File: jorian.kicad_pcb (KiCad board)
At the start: 2 copper layers, 99.1 x 99.7 mm, 107 parts, among them J1 MicroUSB, J2 USB-C, J3 MicroUSB, J4 USB-C, J5 MJ-4PP-9, SW1 SW_SPDT, U3 AMS1117, U4 TP4056, U5 DW01A, U6 FS8205A

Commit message: updated placement
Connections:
- J4 pad A6: D+ -> Net-(J4-PadA6)
- J4 pad A7: D- -> Net-(J4-PadA7)
- J4 pad B6: D+ -> Net-(J4-PadA6)
- J4 pad B7: D- -> Net-(J4-PadA7)
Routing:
- net VCC: track 608.3 -> 683.9 mm, vias 28 -> 23
- net Net-(JP4-Pad2): track 84.2 -> 149.1 mm, vias 2 -> 3
- net SCL: track 139.5 -> 94.7 mm, vias 11 -> 3
- net LIPO+: track 76.6 -> 113.3 mm, vias 3 -> 7
- net /S2: track 110.6 -> 77.9 mm, vias 7 -> 5
- net /S5: track 111.5 -> 79.8 mm, vias 6 -> 4
- net /S21: track 91.5 -> 109.7 mm
- net Net-(JP3-Pad2): track 131.8 -> 145.8 mm
- net /S12: track 47.7 -> 35.2 mm, vias 3 -> 2
- net /S18: track 63.5 -> 51.3 mm, vias 3 -> 2
- net Net-(L7-Pad1): track 36.0 -> 48.0 mm, vias 3 -> 2
- net SWO: track 56.6 -> 45.6 mm
- net /S19: track 126.2 -> 116.5 mm, vias 4 -> 3
- net /DIN18: track 13.6 -> 21.8 mm, vias 1 -> 0
- net Net-(U5-Pad1): track 32.2 -> 40.3 mm
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
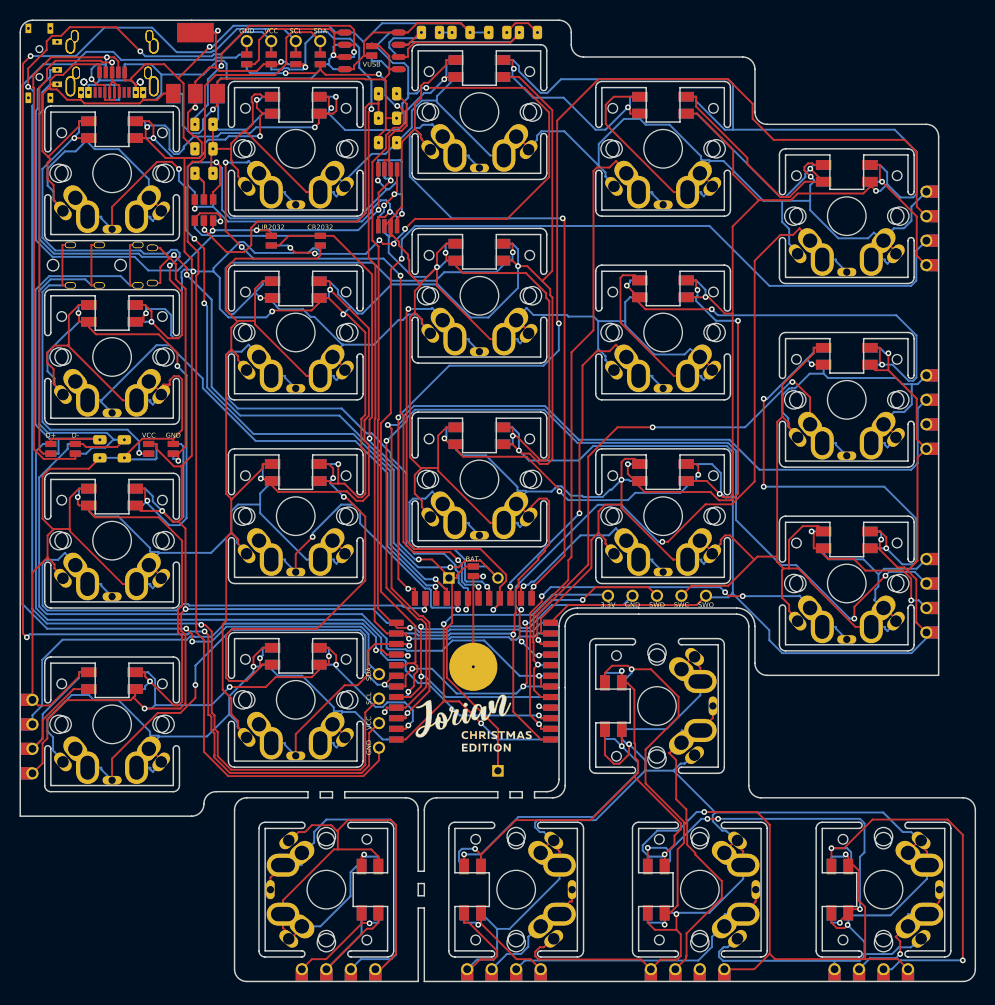
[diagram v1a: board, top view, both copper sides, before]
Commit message: separate charger
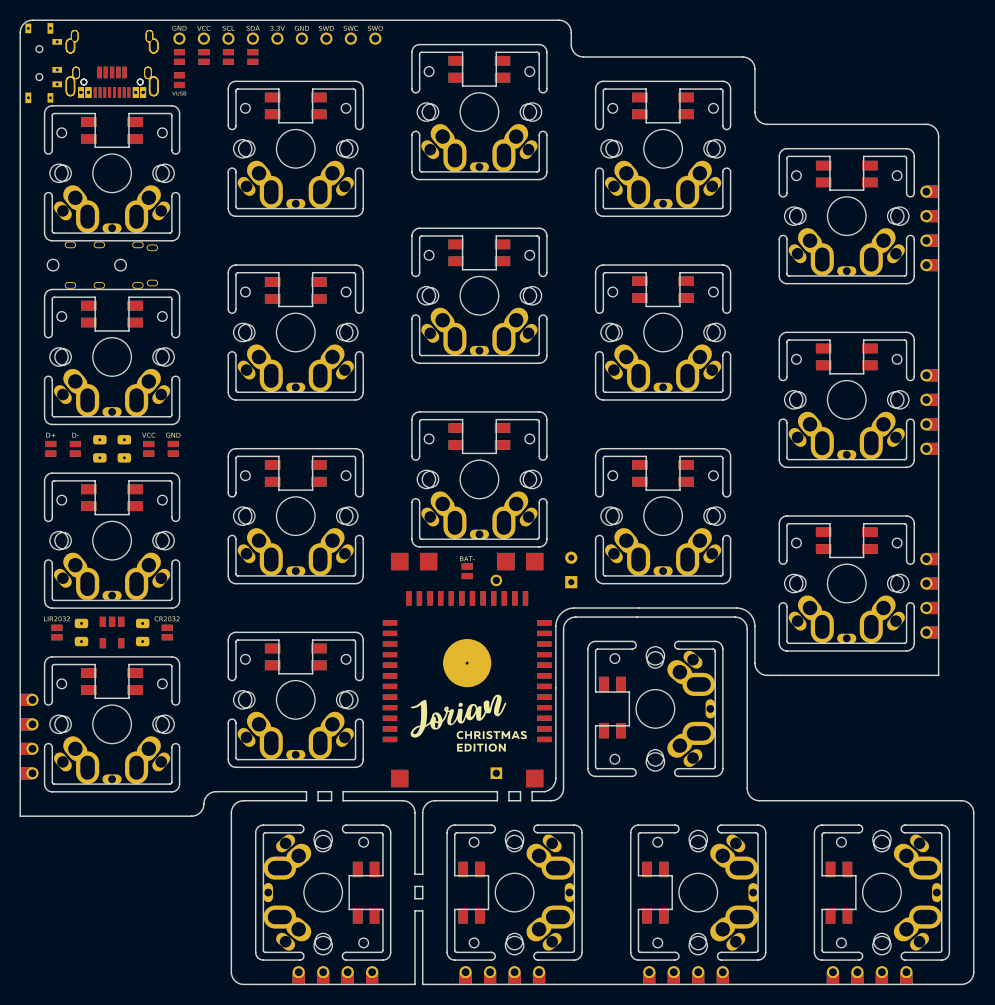
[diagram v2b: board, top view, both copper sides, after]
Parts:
- removed C3, C4: 0.1uF, kbd:C_0805
- removed C5: 10uF, kbd:C_0805
- removed D1, D2: LED, kbd:R_0805
- removed OLED2: I2C_conn, kbd:connector_i2c
- removed R1: 1.2K, kbd:R_0805
- removed R2, R6, R7: 1K, kbd:R_0805
- removed R3: 100, kbd:R_0805
- removed U4: TP4056, kbd:SOP-8
- removed U5: DW01A, kbd:SOT-23-6
- removed U6: FS8205A, kbd:TSSOP-8
- added C1: 1nF, kbd:C_0805, F.Cu at (47.6, 102.2)
- added C2: 1nF, kbd:C_0805, F.Cu at (54.0, 102.2)
- added J6: lipo_charger, kbd:lipo_charger_03962A, F.Cu at (87.6, 119.4)
- added J7: lipo_header, kbd:lipo_header, F.Cu at (98.4, 95.8)
- U3: value AMS1117 -> LP3990-3.3v; footprint kbd:SOT-223-3 -> kbd:SOT-23-5
- moved JP16 67.2 mm to (71.8, 40.6)
- moved U3 59.7 mm to (50.8, 102.2), turned to 270 degrees
- moved JP18 46.3 mm to (45.1, 102.2)
- moved JP19 46.3 mm to (45.1, 102.2)
- moved JP20 43.6 mm to (56.5, 102.2)
- moved JP21 43.6 mm to (56.5, 102.2)
- moved JP15 20.2 mm to (57.8, 45.0)
- moved JP17 20.2 mm to (57.8, 45.0)
- moved JP2 6.99 mm to (57.8, 42.5)
- moved JP3 6.99 mm to (60.3, 42.5)
- moved JP5 6.99 mm to (65.4, 42.5)
- moved JP6 6.99 mm to (57.8, 42.5)
- moved JP7 6.99 mm to (60.3, 42.5)
- moved JP9 6.99 mm to (65.4, 42.5)
- moved OLED1 6.99 mm to (61.6, 40.6)
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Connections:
- JP15 pad 1: VUSB -> OUT+
- JP15 pad 2: LIPO+ -> VUSB
- JP17 pad 1: VUSB -> OUT+
- JP17 pad 2: LIPO+ -> VUSB
- U3 pad 1: GND -> OUT+
- U3 pad 2: VCC -> GND
- U3 pad 3: LIPO+ -> OUT+
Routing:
- net GND: track 1088.0 -> 0.00 mm, vias 6 -> 0
- net VCC: track 683.9 -> 0.00 mm, vias 23 -> 0
- net /GND_B: track 214.4 -> 0.00 mm, vias 3 -> 0
- net Net-(JP4-Pad2): track 149.1 -> 0.00 mm, vias 3 -> 0
- net Net-(JP3-Pad2): track 145.8 -> 0.00 mm, vias 3 -> 0
- net Net-(JP2-Pad2): track 125.4 -> 0.00 mm, vias 2 -> 0
- net /VCC_B: track 122.7 -> 0.00 mm, vias 5 -> 0
- net /S19: track 116.5 -> 0.00 mm, vias 3 -> 0
- net /S20: track 116.1 -> 0.00 mm, vias 2 -> 0
- net LIPO+: track 113.3 -> 0.00 mm, vias 7 -> 0
- net Net-(JP5-Pad2): track 111.4 -> 0.00 mm
- net /S21: track 109.7 -> 0.00 mm, vias 4 -> 0
- net /S22: track 103.2 -> 0.00 mm, vias 2 -> 0
- net SCL: track 94.7 -> 0.00 mm, vias 3 -> 0
- net SDA: track 94.0 -> 0.00 mm, vias 4 -> 0
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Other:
- board size 99.1 x 99.7 mm -> 98.9 x 100 mm
- net class Default: clearance 0.127 -> 0.15
- rule trace_clearance: 0.127 -> 0.15

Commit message: sent files
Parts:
- C1, C2: value 1nF -> 1uF
- J7: value lipo_header -> Conn_01x02
- JP1: value BAT+ -> B+
- JP10: value BAT- -> B-
- JP15, JP17: value VUSB -> 5V
- moved J7 28.8 mm to (69.8, 99.7)
- moved JP18 20.5 mm to (65.4, 99.7)
- moved JP19 20.5 mm to (65.4, 99.7)
- moved JP20 18.0 mm to (74.3, 99.7)
- moved JP21 18.0 mm to (74.3, 99.7)
- moved C1 8.26 mm to (55.9, 102.2)
- moved C2 8.26 mm to (45.7, 102.2)
- moved JP1 1.08 mm to (87.6, 94.8)
- moved JP10 1.08 mm to (87.6, 94.8)
- moved JP15 0.77 mm to (57.8, 45.7), turned to 180 degrees
- moved JP17 0.77 mm to (57.8, 45.7), turned to 0 degrees
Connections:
- net /SWC renamed SWC
- net /SWD renamed SWD
- J6 pad 6: OUT- -> GND
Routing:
- net GND: track 0.00 -> 1118.3 mm, vias 0 -> 13
- net VCC: track 0.00 -> 656.5 mm, vias 0 -> 27
- net /GND_B: track 0.00 -> 225.2 mm, vias 0 -> 4
- net OUT+: track 0.00 -> 167.9 mm, vias 0 -> 6
- net SDA: track 0.00 -> 164.6 mm, vias 0 -> 6
- net /VCC_B: track 0.00 -> 132.2 mm, vias 0 -> 7
- net VUSB: track 0.00 -> 127.6 mm, vias 0 -> 2
- net /S1: track 0.00 -> 112.2 mm, vias 0 -> 6
- net /S19: track 0.00 -> 106.9 mm, vias 0 -> 6
- net Net-(BT1-Pad1): track 0.00 -> 105.5 mm, vias 0 -> 1
- net /S20: track 0.00 -> 102.7 mm, vias 0 -> 6
- net LIPO-: track 0.00 -> 102.1 mm, vias 0 -> 8
- net SWO: track 0.00 -> 101.5 mm, vias 0 -> 1
- net BAT+: track 0.00 -> 94.8 mm, vias 0 -> 1
- net SWD: track 0.00 -> 94.0 mm, vias 0 -> 1
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
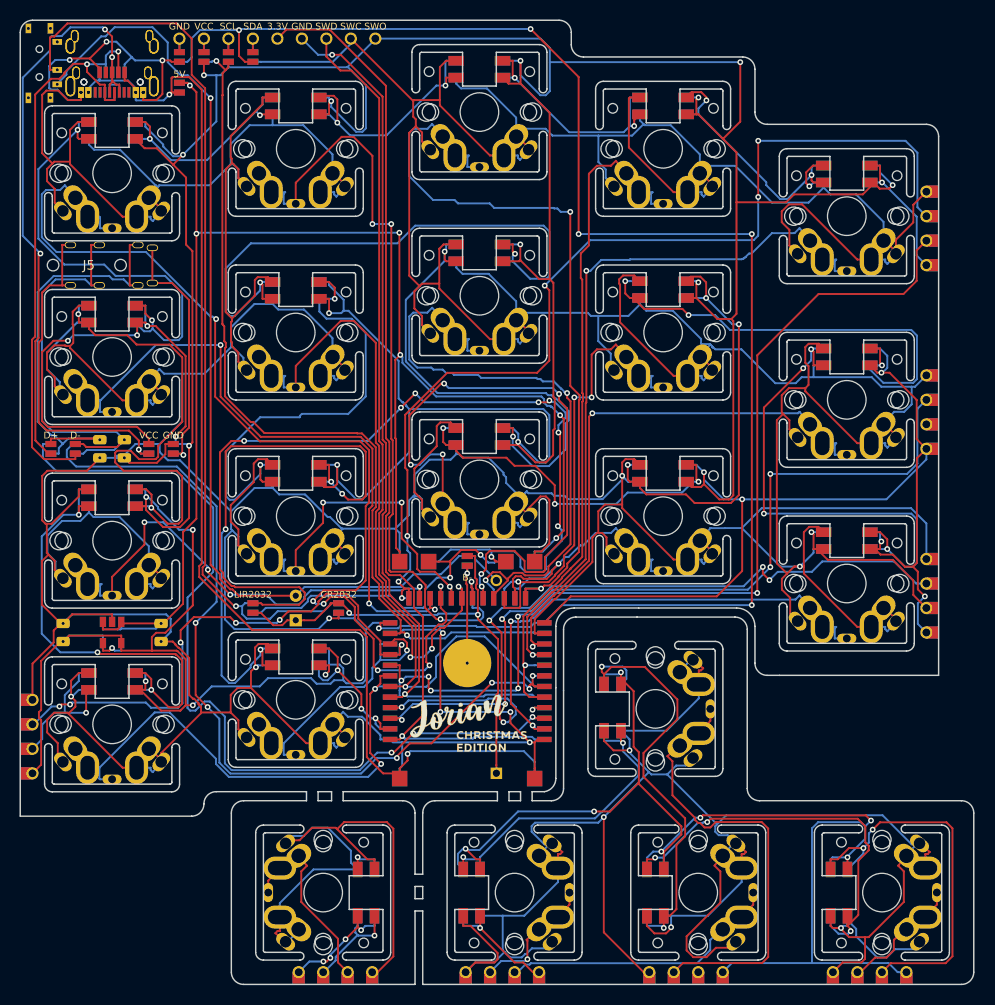
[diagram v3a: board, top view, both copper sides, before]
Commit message: charger with holes, autorouted
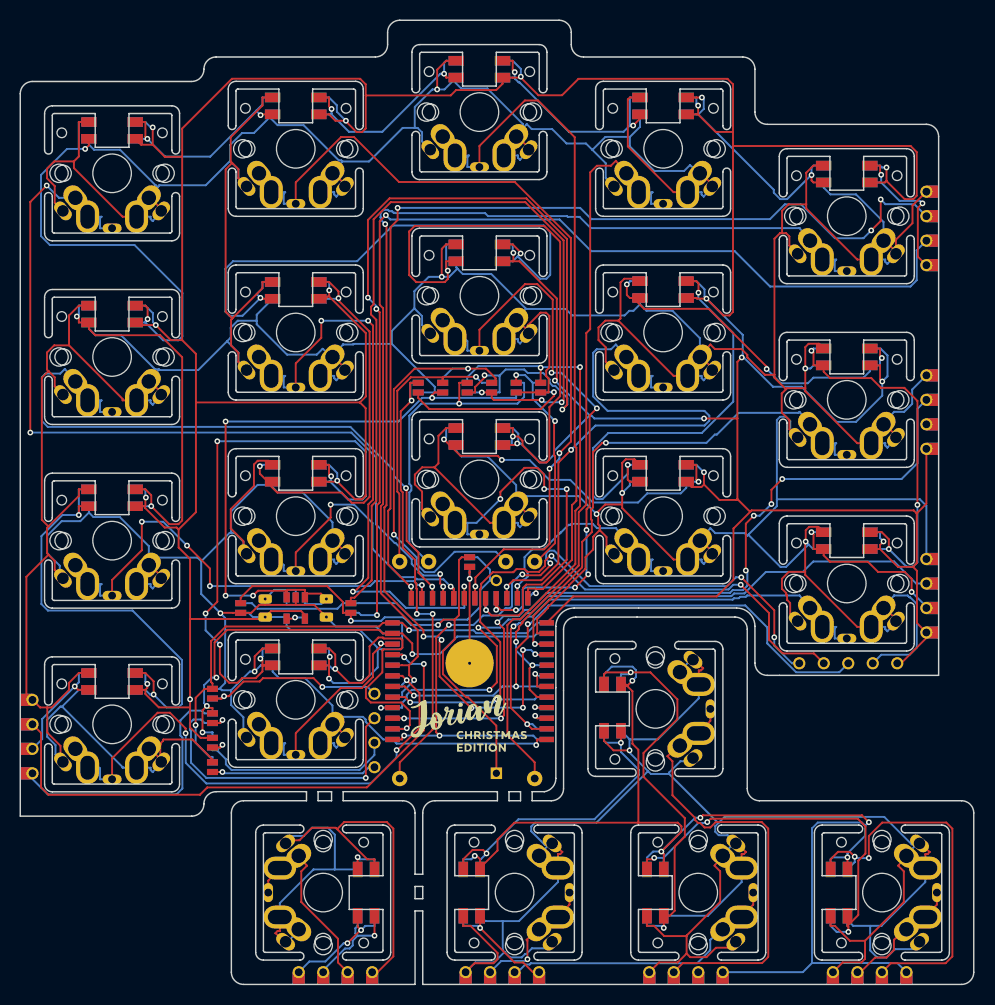
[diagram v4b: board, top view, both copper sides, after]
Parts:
- removed J1, J3: MicroUSB, kbd:usb_micro_custom
- removed J2, J4: USB-C, kbd:usb_type_c
- removed J5: MJ-4PP-9, kbd:trrs_connector
- removed J7: Conn_01x02, kbd:lipo_header
- removed R4, R5: 1.5K, kbd:R_0805
- removed SW1: SW_SPDT, kbd:switch_MSK-12C02_smd
- added JP26: LIPO-, kbd:jumper, B.Cu at (87.6, 76.8)
- added JP27: OUT-, kbd:jumper, B.Cu at (82.5, 76.8)
- JP1: value B+ -> +
- JP10: value B- -> -
- JP11: value VCC -> VUSB; moved to F.Cu
- JP13: value VCC -> OUT+
- JP14: value GND -> LIPO+; moved to F.Cu
- JP15: value 5V -> LIPO-
- JP17: value 5V -> OUT-; moved to F.Cu
- JP18: value LIR2032 -> LIPO+
- JP19: value LIR2032 -> LIPO-
- JP20: value CR2032 -> BAT+
- JP21: value CR2032 -> BAT-
- JP22: value D+ -> VUSB; moved to B.Cu
- JP23: value D- -> GND; moved to B.Cu
- JP24: value TX -> OUT+
- JP25: value RX -> LIPO+
- moved JP16 84.4 mm to (125.9, 105.4)
- moved JP2 73.7 mm to (61.2, 116.2), turned to 180 degrees
- moved JP6 73.7 mm to (61.2, 116.2), turned to 0 degrees
- moved OLED1 73.6 mm to (78.0, 112.4), turned to 270 degrees
- moved JP3 71.1 mm to (61.2, 113.7), turned to 180 degrees
- moved JP7 71.1 mm to (61.2, 113.7), turned to 0 degrees
- moved JP4 68.6 mm to (61.2, 111.1), turned to 180 degrees
- moved JP8 68.6 mm to (61.2, 111.1), turned to 0 degrees
- moved JP5 66.2 mm to (61.2, 108.6), turned to 180 degrees
- moved JP9 66.2 mm to (61.2, 108.6), turned to 0 degrees
- moved JP22 51.2 mm to (95.2, 76.8)
- moved JP24 48.7 mm to (92.7, 76.8), turned to 180 degrees
- moved JP17 46.8 mm to (92.7, 76.8)
- moved JP15 44.9 mm to (90.2, 76.8), turned to 0 degrees
- moved JP25 43.6 mm to (90.2, 76.8), turned to 180 degrees
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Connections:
- BT1 pad 1: Net-(BT1-Pad1) -> BAT+
- J6 pad 1: VUSB -> Net-(J6-Pad1)
- J6 pad 2: GND -> Net-(J6-Pad2)
- J6 pad 3: OUT+ -> Net-(J6-Pad3)
- J6 pad 4: LIPO+ -> Net-(J6-Pad4)
- J6 pad 5: LIPO- -> Net-(J6-Pad5)
- J6 pad 6: GND -> Net-(J6-Pad6)
- JP1 pad 2: Net-(BT1-Pad1) -> BAT+
- JP11 pad 1: Net-(J5-PadA) -> VUSB
- JP11 pad 2: VCC -> Net-(J6-Pad1)
- JP12 pad 1: Net-(J5-PadA) -> GND
- JP12 pad 2: GND -> Net-(J6-Pad2)
- JP13 pad 1: Net-(J5-PadB) -> OUT+
- JP13 pad 2: VCC -> Net-(J6-Pad3)
- JP14 pad 1: Net-(J5-PadB) -> LIPO+
- JP14 pad 2: GND -> Net-(J6-Pad4)
- JP15 pad 1: OUT+ -> LIPO-
- JP15 pad 2: VUSB -> Net-(J6-Pad5)
- JP17 pad 1: OUT+ -> GND
- JP17 pad 2: VUSB -> Net-(J6-Pad6)
- JP22 pad 1: Net-(J5-PadD) -> VUSB
- JP22 pad 2: D+ -> Net-(J6-Pad6)
- JP23 pad 1: Net-(J5-PadC) -> GND
- JP23 pad 2: D- -> Net-(J6-Pad5)
- JP24 pad 1: TX -> OUT+
- JP24 pad 2: Net-(J5-PadD) -> Net-(J6-Pad4)
- JP25 pad 1: RX -> LIPO+
- JP25 pad 2: Net-(J5-PadC) -> Net-(J6-Pad3)
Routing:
- net GND: track 1118.3 -> 973.9 mm, vias 13 -> 9
- net SDA: track 164.6 -> 51.3 mm, vias 6 -> 2
- net VUSB: track 127.6 -> 17.5 mm, vias 2 -> 1
- net Net-(BT1-Pad1): track 105.5 -> 0.00 mm, vias 1 -> 0
- net OUT+: track 167.9 -> 69.5 mm, vias 6 -> 4
- net TX: track 90.9 -> 2.68 mm, vias 3 -> 1
- net RX: track 89.1 -> 3.67 mm, vias 6 -> 1
- net VCC: track 656.5 -> 587.3 mm, vias 27 -> 22
- net LIPO+: track 35.0 -> 102.9 mm, vias 2 -> 5
- net D-: track 63.0 -> 0.00 mm, vias 2 -> 0
- net D+: track 62.5 -> 0.00 mm, vias 3 -> 0
- net Net-(J6-Pad2): track 0.00 -> 61.8 mm, vias 0 -> 2
- net BAT+: track 94.8 -> 34.2 mm, vias 1 -> 0
- net Net-(J6-Pad1): track 0.00 -> 48.9 mm, vias 0 -> 3
- net /S5: track 77.1 -> 124.2 mm, vias 2 -> 7
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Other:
- outline, holes or cut-outs redrawn

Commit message: updated layout
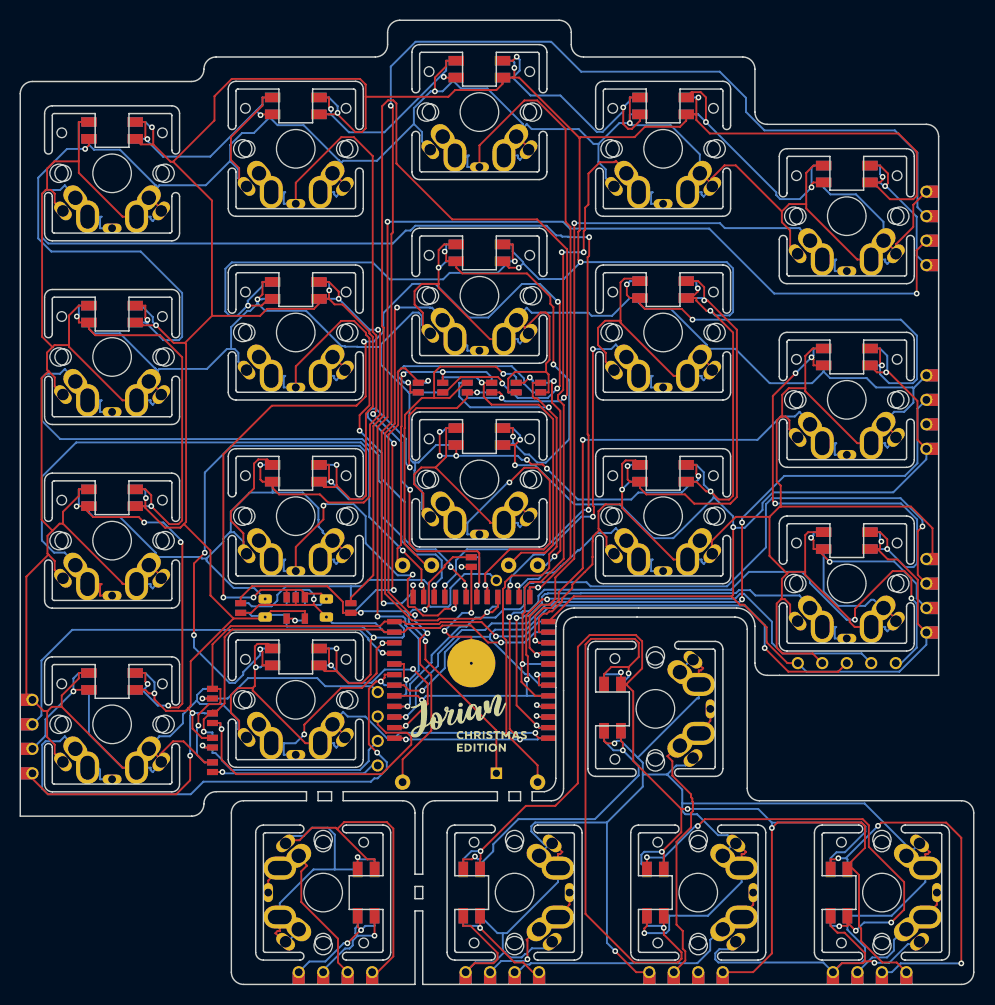
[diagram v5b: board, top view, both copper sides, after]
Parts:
- moved JP16 2.39 mm to (128.3, 105.4), turned to 180 degrees
- moved J6 0.48 mm to (87.9, 119.8)
- moved OLED1 0.38 mm to (78.3, 112.2)
- moved U1 0.22 mm to (88.1, 106.6)
- moved U2 0.22 mm to (88.1, 106.6)
- moved JP1 0.18 mm to (88.1, 94.9)
- moved H1 0.18 mm to (88.1, 105.4)
- moved JP10 0.18 mm to (88.1, 94.9)
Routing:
- net LIPO+: track 102.9 -> 49.0 mm, vias 5 -> 4
- net /S5: track 124.2 -> 81.7 mm, vias 7 -> 2
- net OUT+: track 69.5 -> 107.6 mm, vias 4 -> 6
- net /S1: track 93.2 -> 123.4 mm, vias 4 -> 3
- net /S19: track 105.5 -> 131.8 mm, vias 4 -> 3
- net /S9: track 65.4 -> 42.7 mm, vias 2 -> 3
- net Net-(L13-Pad3): track 64.5 -> 42.7 mm, vias 2 -> 3
- net /VCC_B: track 132.6 -> 154.3 mm, vias 6 -> 5
- net /S11: track 51.3 -> 72.2 mm, vias 4 -> 2
- net Net-(L20-Pad1): track 43.1 -> 63.2 mm
- net LIPO-: track 91.0 -> 110.4 mm, vias 3 -> 2
- net /S22_B: track 48.4 -> 33.5 mm
- net /S18: track 62.9 -> 48.5 mm, vias 2 -> 1
- net /S2: track 88.6 -> 75.0 mm
- net Net-(L7-Pad1): track 62.8 -> 49.6 mm
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
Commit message: edge cuts 0.2 tolerance 0.175
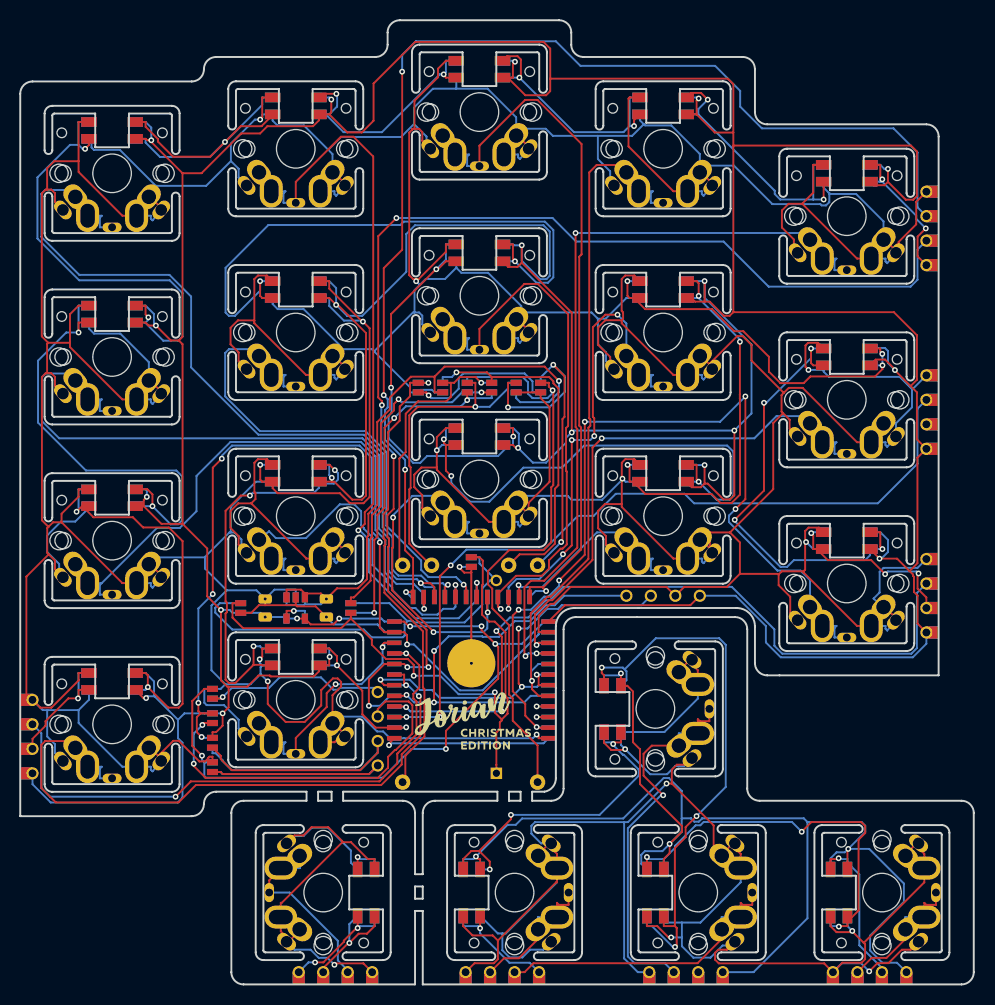
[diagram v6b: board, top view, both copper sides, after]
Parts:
- moved JP16 21.5 mm to (108.0, 98.4)
- moved G1 0.49 mm to (88.1, 111.1)
- moved G2 0.43 mm to (88.1, 111.4)
- moved L22 0.14 mm to (102.8, 110.2)
- moved L5 0.08 mm to (127.0, 54.7)
- moved L7 0.08 mm to (69.8, 66.8)
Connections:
- JP16 pad 1: SWO -> VCC
- JP16 pad 2: SWC -> GND
- JP16 pad 4: GND -> SWC
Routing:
- net LIPO-: track 110.4 -> 33.6 mm
- net SWO: track 88.8 -> 17.8 mm, vias 5 -> 1
- net SCL: track 48.3 -> 90.9 mm, vias 2 -> 6
- net OUT+: track 107.6 -> 65.3 mm, vias 6 -> 1
- net /S1: track 123.4 -> 85.5 mm, vias 3 -> 1
- net /S15: track 53.9 -> 91.0 mm, vias 2 -> 6
- net VCC: track 586.6 -> 611.7 mm, vias 24 -> 23
- net SWD: track 64.9 -> 41.8 mm, vias 2 -> 3
- net /DIN21_B: track 41.0 -> 18.1 mm, vias 3 -> 1
- net SWC: track 65.8 -> 44.3 mm
- net Net-(L12-Pad3): track 64.4 -> 44.0 mm, vias 4 -> 3
- net Net-(JP3-Pad2): track 22.6 -> 40.7 mm, vias 1 -> 0
- net Net-(JP2-Pad2): track 18.6 -> 35.2 mm, vias 1 -> 0
- net SDA: track 53.1 -> 69.6 mm, vias 2 -> 5
- net Net-(L13-Pad1): track 38.3 -> 54.3 mm, vias 6 -> 3
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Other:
- net class Default: clearance 0.15 -> 0.175
- rule trace_clearance: 0.15 -> 0.175
